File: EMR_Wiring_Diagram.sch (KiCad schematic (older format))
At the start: 11 parts, among them SW1 Emergency Switch, SW2 Ignition Key

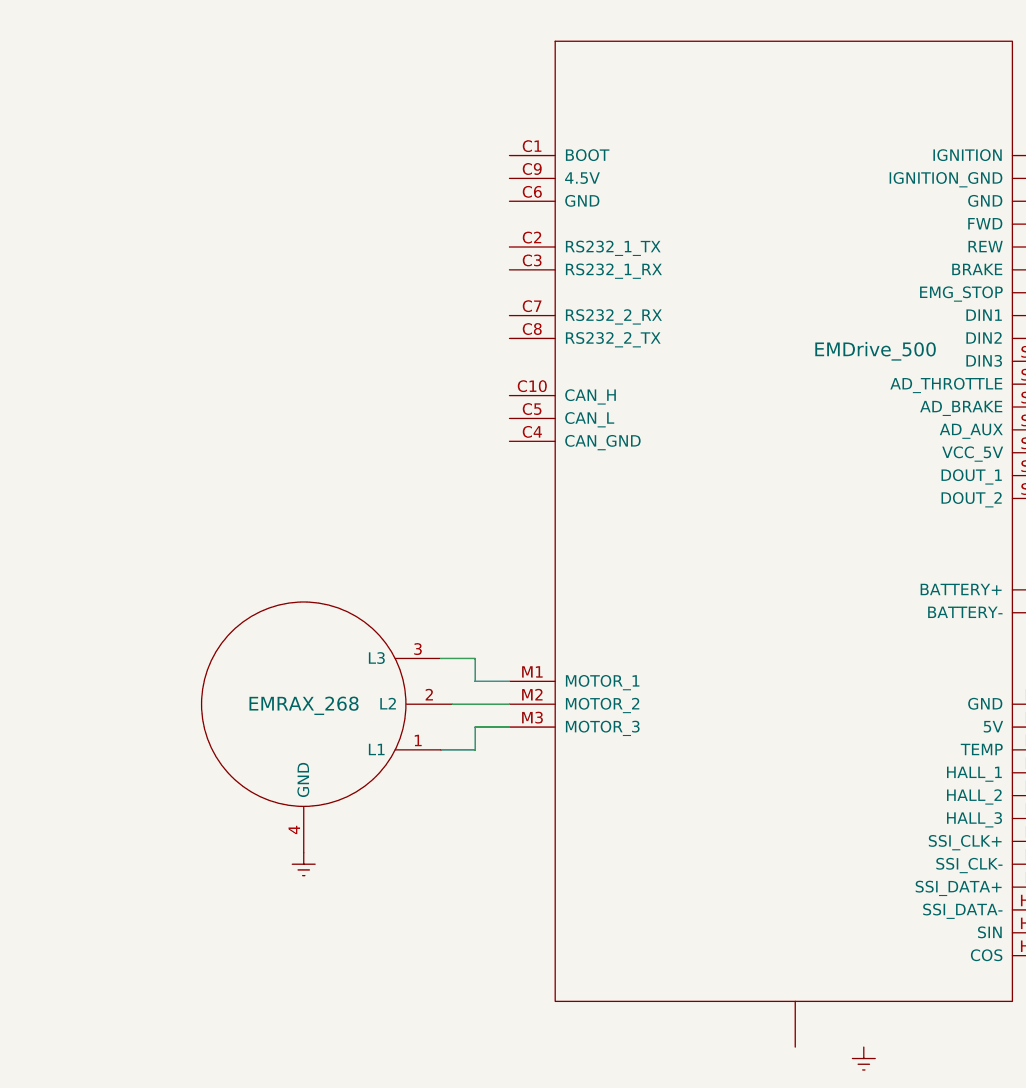
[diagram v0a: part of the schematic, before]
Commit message: Added Display
Added General Display part
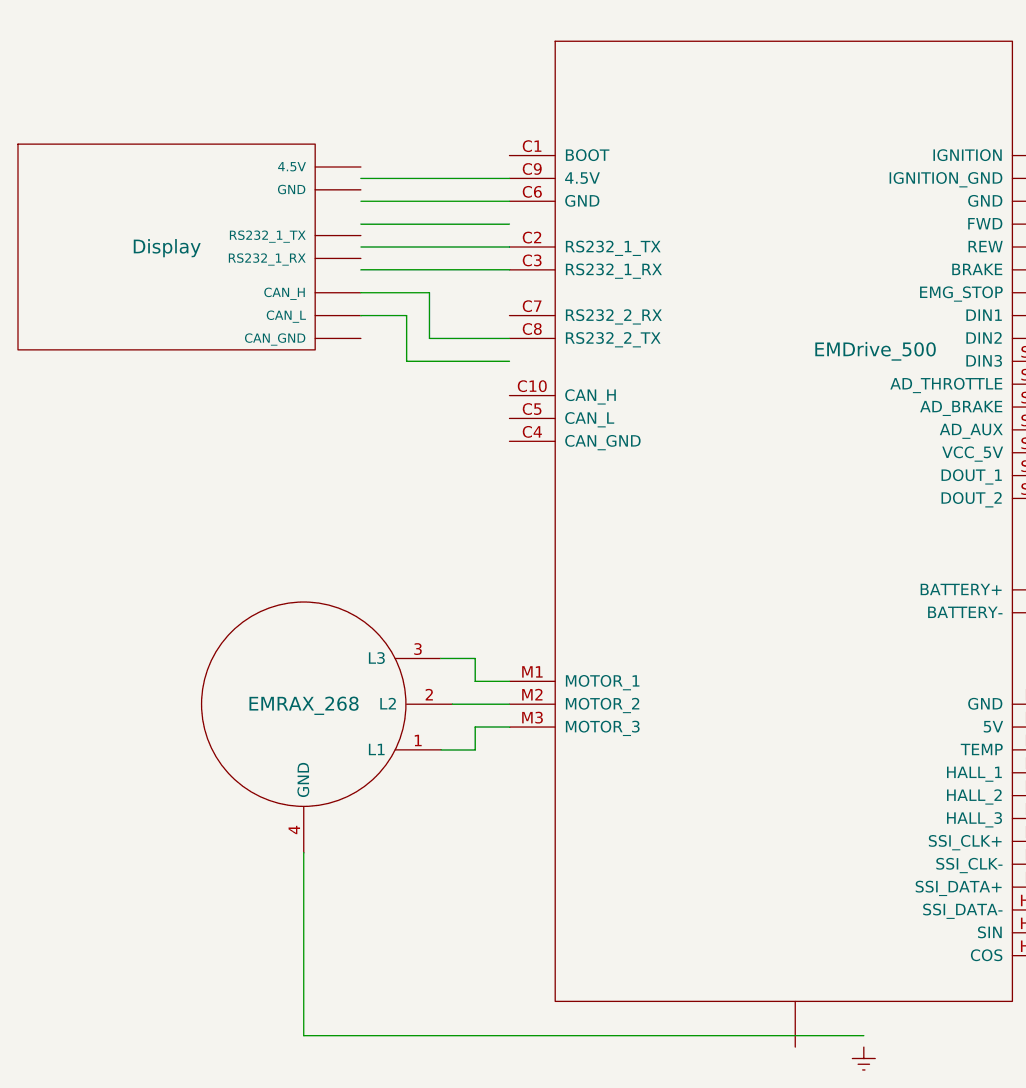
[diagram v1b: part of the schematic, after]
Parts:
- added U?: Display, symbol Display
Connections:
- wire segments 44 -> 57
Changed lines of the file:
@@
 	0    -1   -1   0
-$EndComp
-$Comp
-L Earth #PWR?
-U 1 1 56B15939
-P 3250 4650
-F 0 "#PWR?" H 3250 4400 50  0001 C CNN
-F 1 "Earth" H 3250 4500 50  0001 C CNN
-F 2 "" H 3250 4650 50  0000 C CNN
-F 3 "" H 3250 4650 50  0000 C CNN
-	1    3250 4650
-	1    0    0    -1
 $EndComp
 Wire Wire Line
@@
 Wire Wire Line
 	7600 4200 7150 4200
+Wire Wire Line
+	3250 4650 3250 5450
+Wire Wire Line
+	3250 5450 5700 5450
+$Comp
+L Display U?
+U 1 1 56BFAE42
+P 2650 2000
+F 0 "U?" H 2650 2000 60  0001 C CNN
+F 1 "Display" H 2650 2000 60  0000 C CNN
+F 2 "" H 2650 2000 60  0000 C CNN
+F 3 "" H 2650 2000 60  0000 C CNN
+	1    2650 2000
+	1    0    0    -1
+$EndComp
+Wire Wire Line
+	3500 1700 4150 1700
+Wire Wire Line
+	3500 1800 4150 1800
+Wire Wire Line
+	3500 1900 4150 1900
+Wire Wire Line
+	3500 2000 4150 2000
+Wire Wire Line
+	3500 2100 4150 2100
+Wire Wire Line
+	3500 2200 3800 2200
+Wire Wire Line
+	3800 2200 3800 2400
+Wire Wire Line
+	3800 2400 4150 2400
+Wire Wire Line
+	3500 2300 3700 2300
+Wire Wire Line
+	3700 2300 3700 2500
+Wire Wire Line
+	3700 2500 4150 2500
 $EndSCHEMATC

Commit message: Added sub_schematic for battery/bms
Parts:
- removed U?: Battery_Pack, symbol Battery_Pack
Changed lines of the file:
@@
 $Descr A4 11693 8268
 encoding utf-8
-Sheet 1 1
+Sheet 1 2
 Title "Spark Wiring Diagram"
 Date "2016-01-28"
@@
 $EndComp
 $Comp
-L Battery_Pack U?
-U 1 1 56B0DD37
-P 10200 1600
-F 0 "U?" H 10200 1600 60  0001 C CNN
-F 1 "Battery_Pack" H 10200 1600 60  0000 C CNN
-F 2 "" H 10200 1600 60  0000 C CNN
-F 3 "" H 10200 1600 60  0000 C CNN
-	1    10200 1600
-	-1   0    0    -1
-$EndComp
-$Comp
 L FUSE 4A
 U 1 1 56B0DEE6
@@
 Wire Wire Line
 	3700 2500 4150 2500
+$Sheet
+S 9700 1300 1300 850
+U 56C88E46
+F0 "bat_bms" 60
+F1 "Batterysys.sch" 60
+$EndSheet
 $EndSCHEMATC

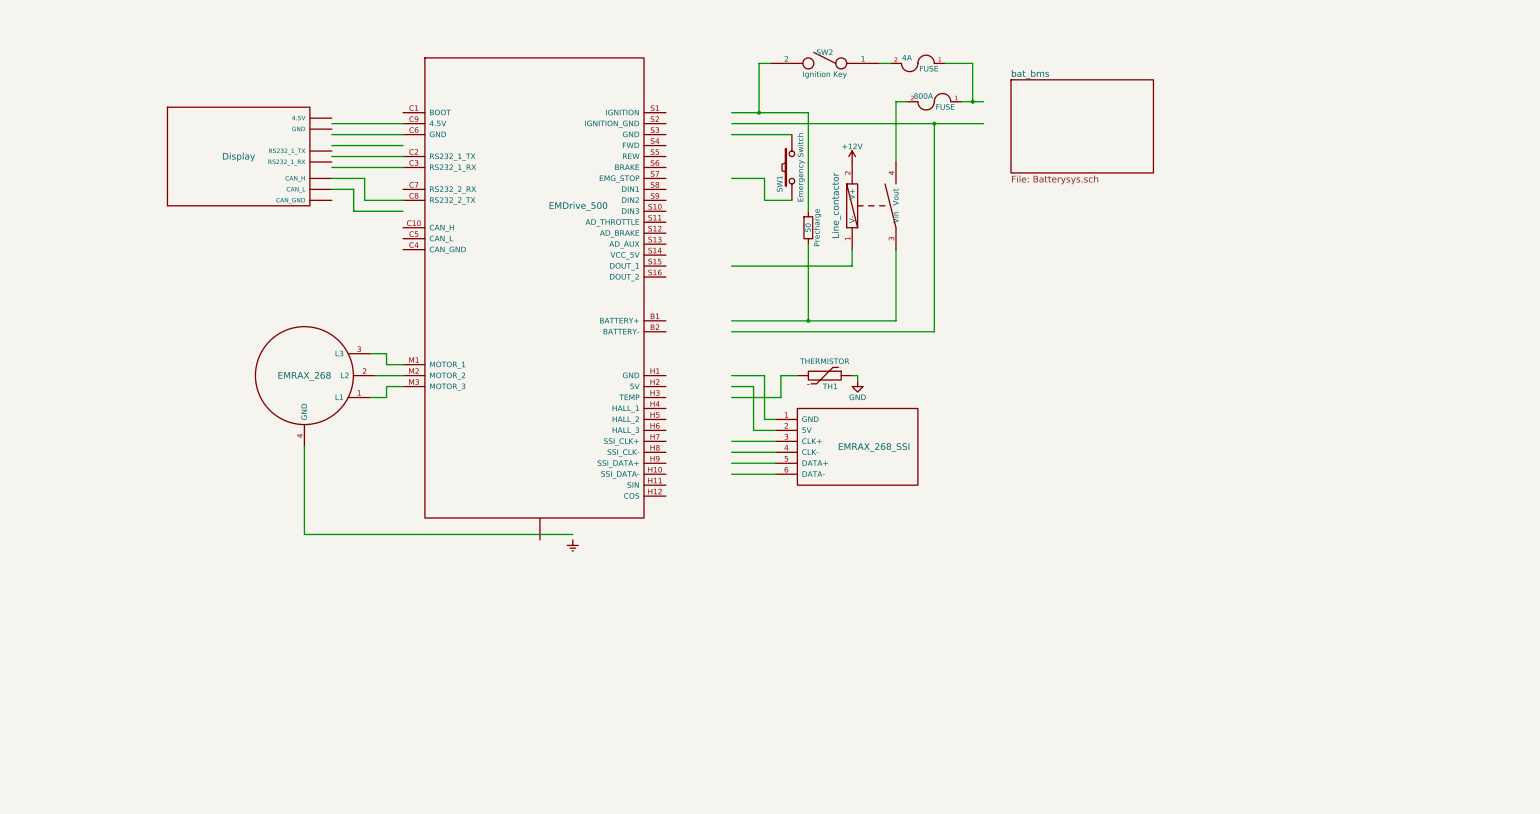
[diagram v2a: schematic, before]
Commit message: Changed Display, finished cell array, added CAN bus
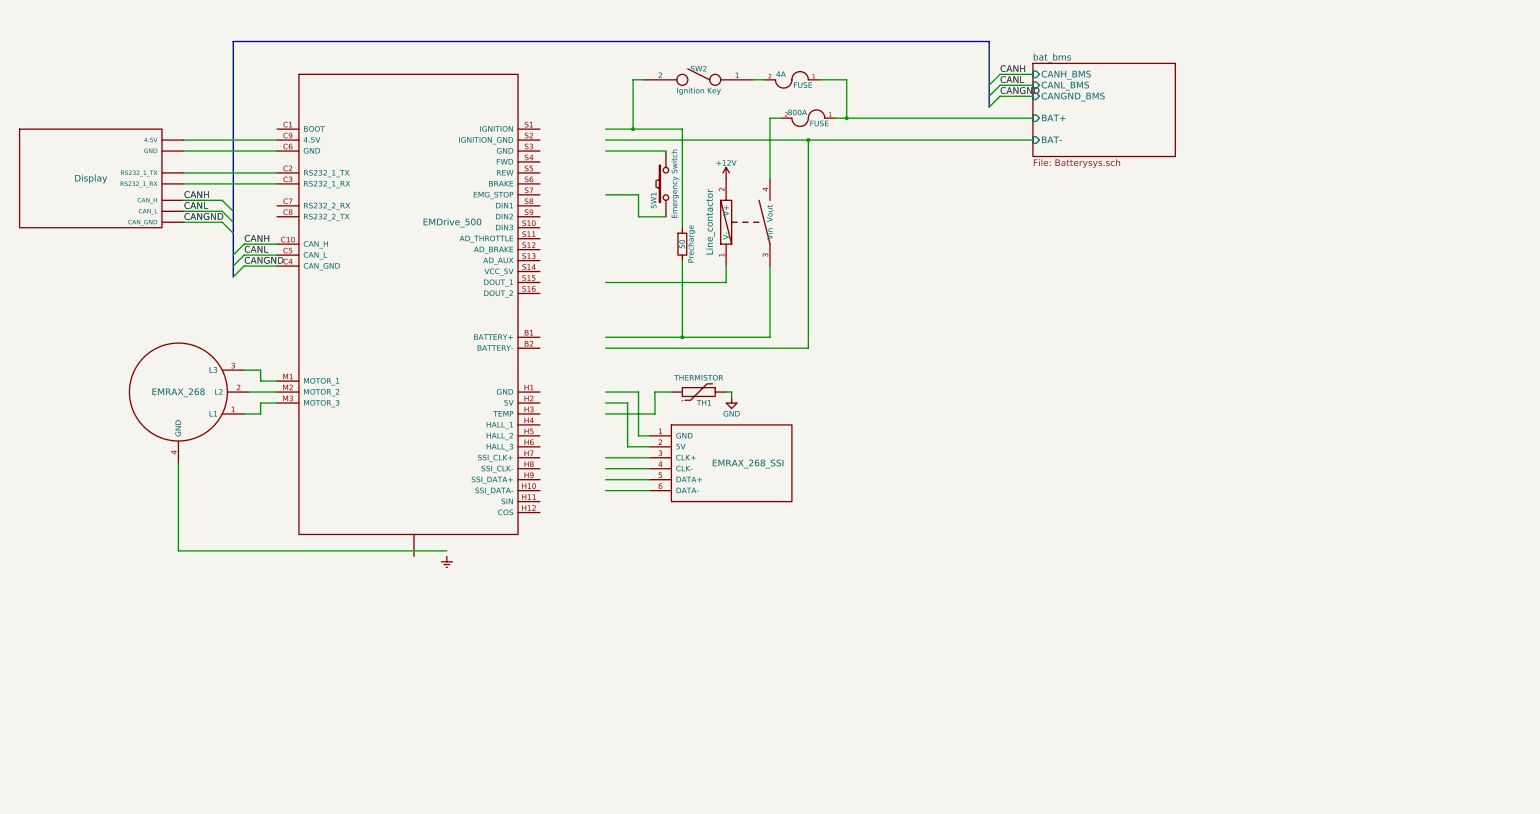
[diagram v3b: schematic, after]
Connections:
- net labels added: CANGND, CANH, CANL
- wire segments 57 -> 59
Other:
- moved on the sheet: 4A, 800A, Precharge, SW1, SW2, TH1

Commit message: Emergency switches and ignition/precharge leds
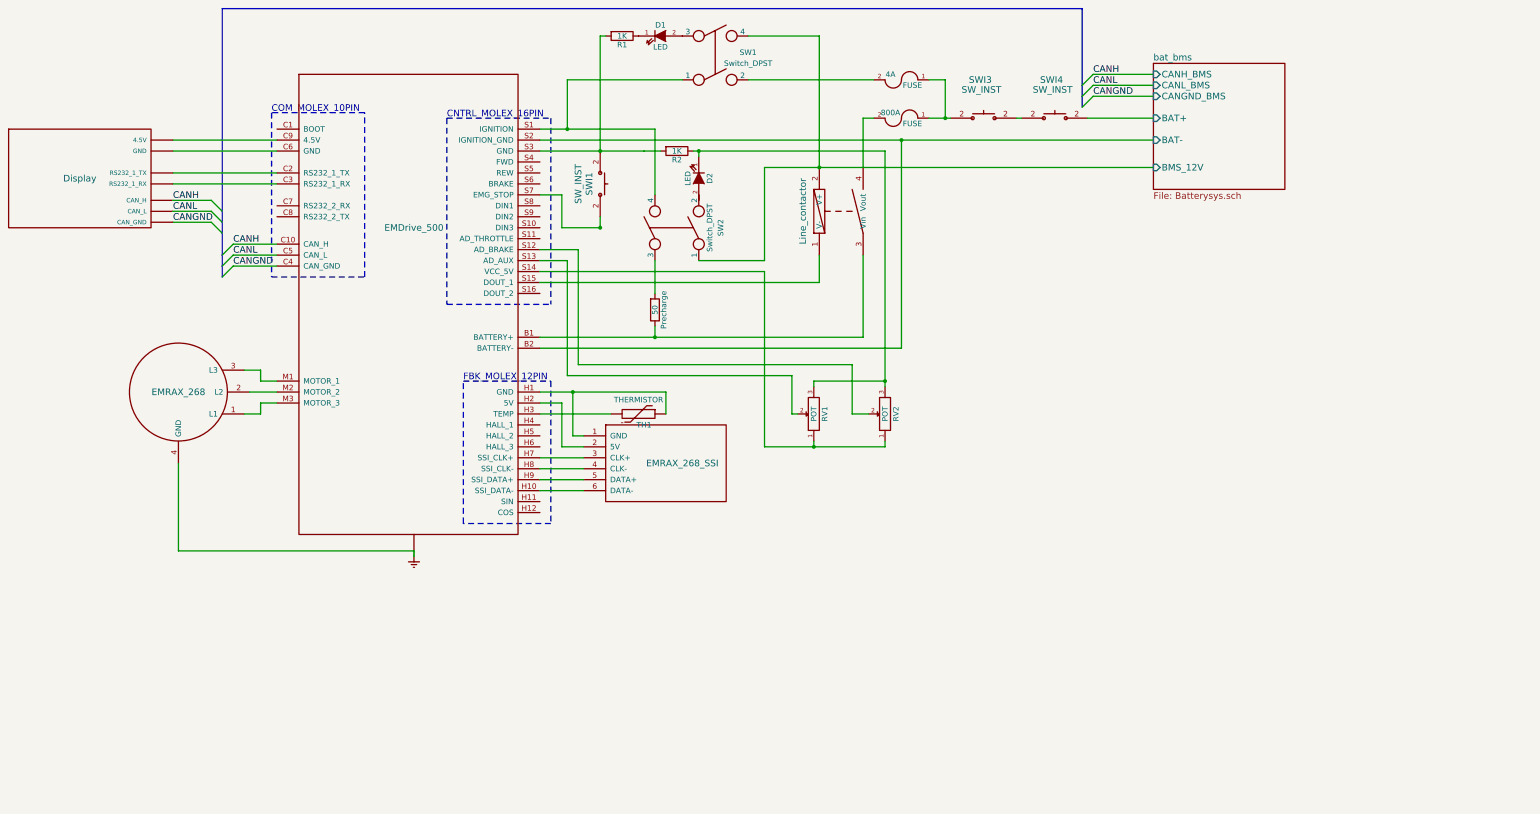
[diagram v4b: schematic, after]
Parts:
- removed SW1: Emergency Switch, symbol SW_PUSH
- removed SW2: Ignition Key, symbol SPST
- added D1, D2: LED, symbol LED
- added R1, R2: 1K, symbol R
- added RV1, RV2: POT, symbol POT
- added SW1, SW2: Switch_DPST, symbol Switch_DPST
- added SWI1, SWI3, SWI4: SW_INST, symbol SW_INST
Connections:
- net labels removed: +12V, GND
- wire segments 59 -> 101
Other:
- note added: "CNTRL_MOLEX_16PIN"
- note added: "COM_MOLEX_10PIN"
- note added: "FBK_MOLEX_12PIN"
- moved on the sheet: 4A, 800A, Precharge, TH1

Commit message: Connector numbering
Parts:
- added SP1: HORN, symbol SPEAKER
- added SWI2: SW_INST, symbol SW_INST
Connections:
- net THROTTLE: now reaches U?.S11 (AD_THROTTLE)
- net THROTTLE: now also RV2.2
- net BRAKE: now reaches U?.S12 (AD_BRAKE)
- net BRAKE: now also RV1.2; no longer RV2.2
- net at U?.S13 (AD_AUX): no longer RV1.2
- net 5V: now reaches RV1.1, RV2.1, U?.S14 (VCC_5V)
- net GND: now reaches R1.2, R2.2, SWI1.2, U?.S3 (GND)
- net GND: now also D2.1 (K), R2.1, RV1.3, RV2.3, SP1.2
- net at SW2.2: now also D2.2 (A)
- net bat_bms/BMS_12V renamed 12V
- net 12V: now also SWI2.2
- new net: SP1.1, SWI2.2
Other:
- note added: "CHASIS_GND\n"
- note added: "CONN10\n"
- note added: "CONN11\n"
- note added: "CONN12\n"
- note added: "CONN13\n"
- note added: "CONN14\n\n"
- note added: "CONN15"
- note added: "CONN16\n"
- note added: "CONN17"
- note added: "CONN18\n"
- note added: "CONN19\n"
- note added: "CONN4\n\n"
- note added: "CONN5\n\n"
- note added: "CONN6"
- note added: "CONN7"
- note added: "CONN8\n"
- note added: "CONN9"
- note removed: "CNTRL_MOLEX_16PIN"
- note removed: "COM_MOLEX_10PIN"
- note removed: "FBK_MOLEX_12PIN"
- moved on the sheet: D2

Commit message: Speaker
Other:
- note added: "CONN20\n"
- moved on the sheet: 4A, 800A, D1, D2, Precharge, R1, R2, RV1, RV2, SP1, SW1, SW2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
